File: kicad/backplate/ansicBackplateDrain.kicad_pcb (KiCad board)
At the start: 2 copper layers, 123 x 102.5 mm, 0 parts

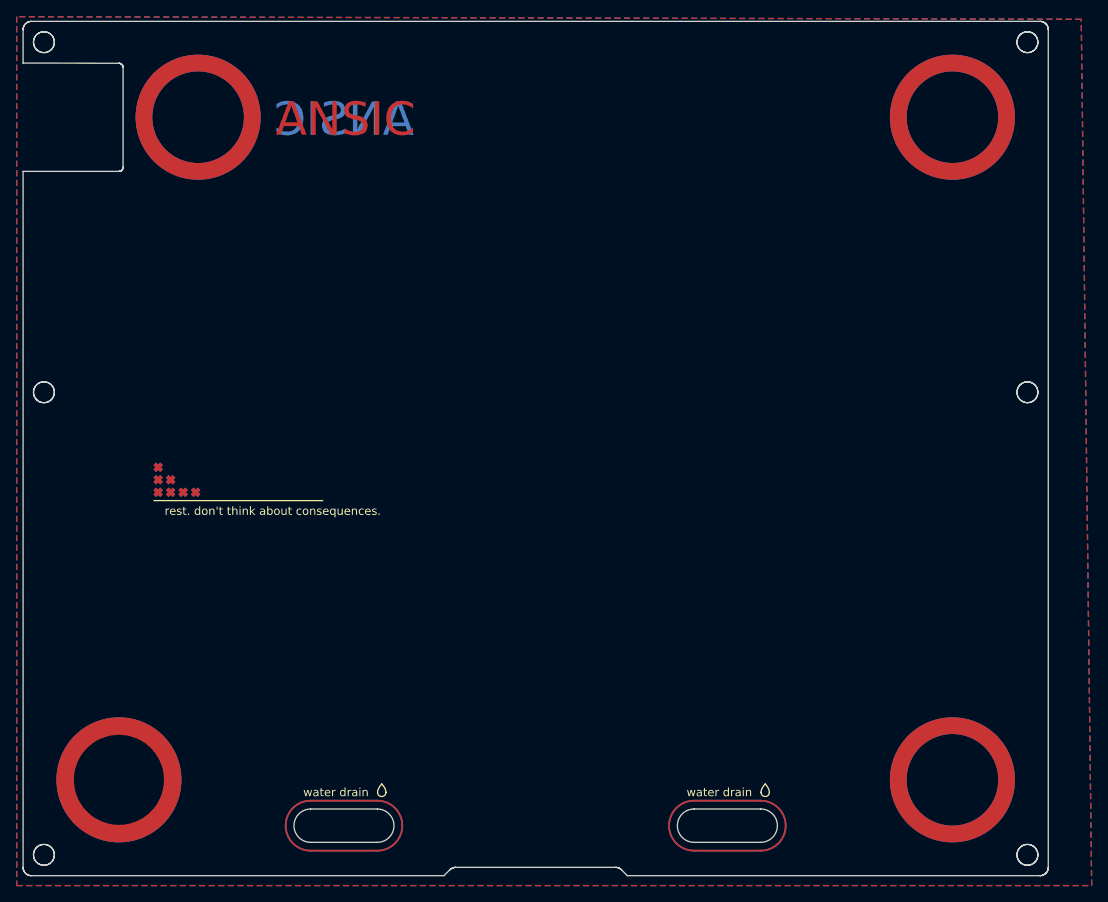
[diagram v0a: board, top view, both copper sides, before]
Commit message: add bumpon and drain footprint
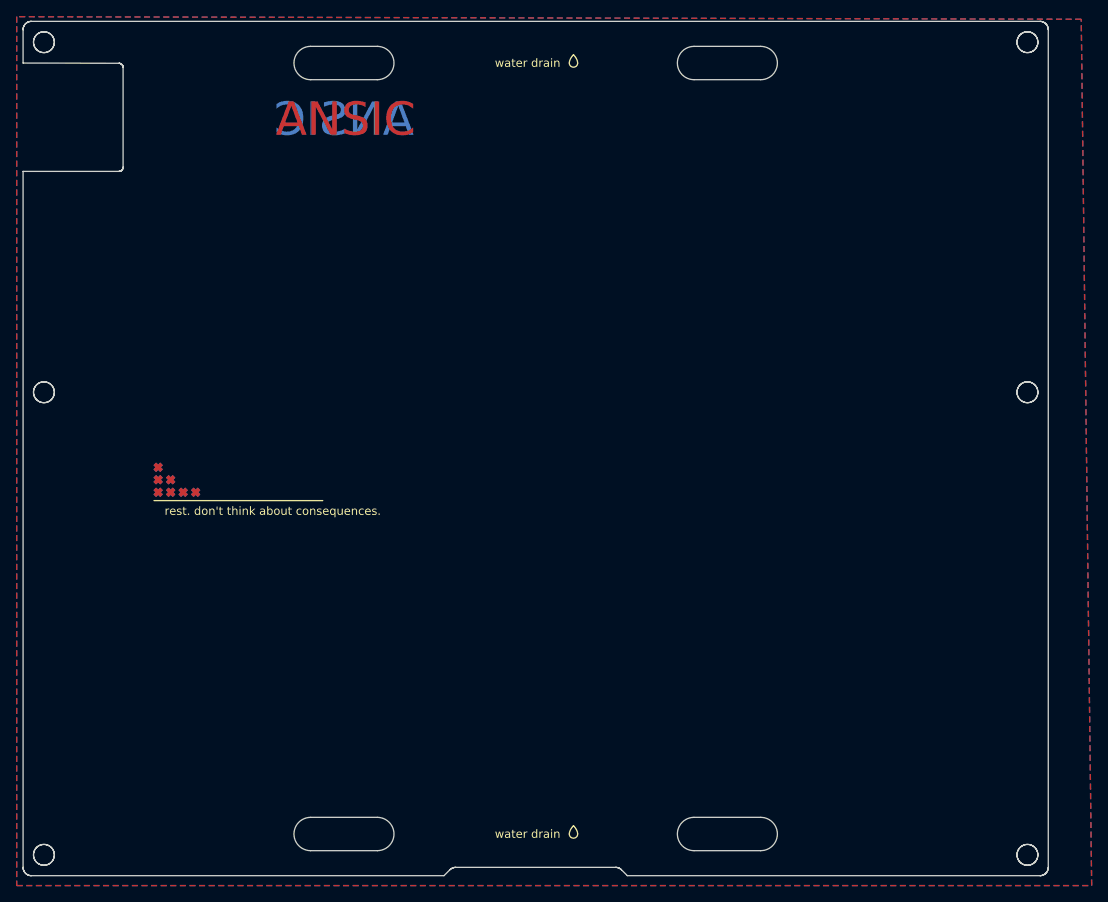
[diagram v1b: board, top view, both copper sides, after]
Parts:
- added REF**: Backplate-BumponGuide-11mm, ansic-CustomFoot:Backplate-BumponGuide-11mm, F.Cu at (169.0, 36.5)
- added REF**: Backplate-WaterDrain, ansic-CustomFoot:Backplate-WaterDrain, F.Cu at (96.0, 30.0)
- added REF**: Backplate-WaterDrain, ansic-CustomFoot:Backplate-WaterDrain, F.Cu at (142.0, 30.0)
- added REF**: Backplate-WaterDrainText, ansic-CustomFoot:Backplate-WaterDrainText, F.Cu at (119.0, 122.5)
- added REF**: Backplate-BumponGuide-11mm, ansic-CustomFoot:Backplate-BumponGuide-11mm, F.Cu at (169.0, 116.0)
- added REF**: Backplate-BumponGuide-11mm, ansic-CustomFoot:Backplate-BumponGuide-11mm, F.Cu at (78.5, 36.5)
- added REF**: Backplate-BumponGuide-11mm, ansic-CustomFoot:Backplate-BumponGuide-11mm, F.Cu at (69.0, 116.0)
- added REF**: Backplate-WaterDrain, ansic-CustomFoot:Backplate-WaterDrain, F.Cu at (142.0, 122.5)
- added REF**: Backplate-WaterDrain, ansic-CustomFoot:Backplate-WaterDrain, F.Cu at (96.0, 122.5)
- added REF**: Backplate-WaterDrainText, ansic-CustomFoot:Backplate-WaterDrainText, F.Cu at (119.0, 30.0)
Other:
- outline, holes or cut-outs redrawn
- board text removed: "water drain"
